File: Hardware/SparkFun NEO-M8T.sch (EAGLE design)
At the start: 51 parts, among them J13 U.FL, J2 Qwiic Right Angle, J4 Qwiic Right Angle, U1 U-BLOX_NEO-M9N, U2 3.3V

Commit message: Some updates to the design (heh)
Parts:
- JP15: device SparkFun-Connectors:CONN_041X04_NO_SILK -> SparkFun-Connectors:CONN_05NO_SILK
- U1: value U-BLOX_NEO-M9N -> U-BLOX_NEO-M8T; device SparkFun-GPS:U-BLOX_NEO-M9N -> SparkFun-GPS:U-BLOX_NEO-M8T
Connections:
- net SCL_LV renamed N$13
- net SDA_LV renamed N$3
- removed net !SAFE: JP15.2, U1.!SAFEBOOT!
- removed net INT: JP15.1, U1.EXT_INT
- new net INT0: JP15.2, U1.EXTINT0
- new net INT1: JP15.1, U1.EXTINT1
- new net TP2/!SAFE: JP15.3, U1.TP2/!SAFEBOOT!
- net !RESET: now also JP15.4; no longer JP15.3
- net PPS: now also JP15.5; no longer JP15.4
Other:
- moved on the sheet: R2, R4
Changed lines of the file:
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@@
 <part name="SUPPLY6" library="SparkFun-PowerSymbols" deviceset="3.3V" device=""/>
 <part name="FB1" library="SparkFun-Coils" deviceset="FERRITE_BEAD" device="-0603" value="30Ω/1.8A"/>
-<part name="JP15" library="SparkFun-Connectors" deviceset="CONN_04" device="1X04_NO_SILK"/>
+<part name="JP15" library="SparkFun-Connectors" deviceset="CONN_05" device="NO_SILK"/>
 <part name="SUPPLY10" library="SparkFun-PowerSymbols" deviceset="3.3V" device=""/>
 <part name="J1" library="SparkFun-Connectors" deviceset="CONN_07" device="NO_SILK"/>
 <part name="SUPPLY11" library="SparkFun-PowerSymbols" deviceset="5V" device=""/>
 <part name="LOGO2" library="SparkFun-Aesthetics" deviceset="SFE_LOGO_NAME_FLAME" device=".1_INCH"/>
-<part name="U1" library="SparkFun-GPS" deviceset="U-BLOX_NEO-M9N" device=""/>
+<part name="U1" library="SparkFun-GPS" deviceset="U-BLOX_NEO-M8T" device=""/>
 <part name="PWR\" library="SparkFun-Jumpers" deviceset="JUMPER-SMT_2_NC_TRACE" device="_SILK" value="JUMPER-SMT_2_NC_TRACE_SILK"/>
 <part name="D3" library="SparkFun-IC-Power" deviceset="PRTR5V0U2" device="F"/>
@@
 </instance>
 <instance part="R3" gate="G$1" x="81.28" y="149.86" smashed="yes">
-<attribute name="NAME" x="76.962" y="150.114" size="1.778" layer="95" font="vector" align="bottom-center"/>
-<attribute name="VALUE" x="85.852" y="150.114" size="1.778" layer="96" font="vector" rot="R180" align="top-center"/>
+<attribute name="NAME" x="76.962" y="147.574" size="1.778" layer="95" font="vector" align="bottom-center"/>
+<attribute name="VALUE" x="85.852" y="147.574" size="1.778" layer="96" font="vector" rot="R180" align="top-center"/>
 </instance>
 <instance part="R6" gate="G$1" x="81.28" y="147.32" smashed="yes">
@@
 <instance part="JP71" gate="G$1" x="233.68" y="27.94" smashed="yes" rot="R270"/>
 <instance part="JP81" gate="G$1" x="236.22" y="27.94" smashed="yes" rot="R270"/>
-<instance part="R2" gate="G$1" x="81.28" y="157.48" smashed="yes">
-<attribute name="NAME" x="77.216" y="158.496" size="1.778" layer="95" font="vector" align="bottom-center"/>
-<attribute name="VALUE" x="85.344" y="158.496" size="1.778" layer="96" font="vector" rot="R180" align="top-center"/>
-</instance>
-<instance part="R4" gate="G$1" x="81.28" y="154.94" smashed="yes">
+<instance part="R2" gate="G$1" x="81.28" y="154.94" smashed="yes">
 <attribute name="NAME" x="76.962" y="152.908" size="1.778" layer="95" font="vector" align="bottom-center"/>
-<attribute name="VALUE" x="85.852" y="152.654" size="1.778" layer="96" font="vector" rot="R180" align="top-center"/>
+<attribute name="VALUE" x="85.598" y="152.908" size="1.778" layer="96" font="vector" rot="R180" align="top-center"/>
+</instance>
+<instance part="R4" gate="G$1" x="81.28" y="152.4" smashed="yes">
+<attribute name="NAME" x="76.962" y="150.368" size="1.778" layer="95" font="vector" align="bottom-center"/>
+<attribute name="VALUE" x="85.852" y="150.114" size="1.778" layer="96" font="vector" rot="R180" align="top-center"/>
 </instance>
 <instance part="SUPPLY1" gate="G$1" x="30.48" y="165.1" smashed="yes" rot="MR0">
@@
 <attribute name="VALUE" x="219.71" y="91.44" size="1.778" layer="96" font="vector" align="top-left"/>
 </instance>
-<instance part="JP15" gate="J1" x="101.6" y="88.9" smashed="yes" rot="MR0">
-<attribute name="VALUE" x="106.68" y="78.74" size="1.778" layer="96" rot="MR0"/>
-<attribute name="NAME" x="106.68" y="97.282" size="1.778" layer="95" font="vector" rot="MR0"/>
+<instance part="JP15" gate="G$1" x="104.14" y="91.44" smashed="yes" rot="MR0">
+<attribute name="VALUE" x="109.22" y="81.28" size="1.778" layer="96" rot="MR0"/>
+<attribute name="NAME" x="109.22" y="99.822" size="1.778" layer="95" font="vector" rot="MR0"/>
 </instance>
 <instance part="SUPPLY10" gate="G$1" x="124.46" y="96.52" smashed="yes">
@@
 <segment>
 <pinref part="R4" gate="G$1" pin="2"/>
-<wire x1="86.36" y1="154.94" x2="88.9" y2="154.94" width="0.1524" layer="91"/>
-<label x="88.9" y="154.94" size="1.27" layer="95" font="vector" xref="yes"/>
+<wire x1="86.36" y1="152.4" x2="88.9" y2="152.4" width="0.1524" layer="91"/>
+<label x="88.9" y="152.4" size="1.27" layer="95" font="vector" xref="yes"/>
 </segment>
 <segment>
@@
 <segment>
 <pinref part="R2" gate="G$1" pin="2"/>
-<wire x1="86.36" y1="157.48" x2="88.9" y2="157.48" width="0.1524" layer="91"/>
-<label x="88.9" y="157.48" size="1.27" layer="95" font="vector" xref="yes"/>
+<wire x1="86.36" y1="154.94" x2="88.9" y2="154.94" width="0.1524" layer="91"/>
+<label x="88.9" y="154.94" size="1.27" layer="95" font="vector" xref="yes"/>
 </segment>
 <segment>
@@
 </segment>
 <segment>
-<wire x1="96.52" y1="91.44" x2="93.98" y2="91.44" width="0.1524" layer="91"/>
-<label x="93.98" y="91.44" size="1.27" layer="95" font="vector" rot="MR0" xref="yes"/>
-<pinref part="JP15" gate="J1" pin="3"/>
-</segment>
-</net>
-<net name="INT" class="0">
+<wire x1="96.52" y1="93.98" x2="93.98" y2="93.98" width="0.1524" layer="91"/>
+<label x="93.98" y="93.98" size="1.27" layer="95" font="vector" rot="MR0" xref="yes"/>
+<pinref part="JP15" gate="G$1" pin="4"/>
+</segment>
+</net>
+<net name="INT0" class="0">
 <segment>
 <wire x1="66.04" y1="160.02" x2="68.58" y2="160.02" width="0.1524" layer="91"/>
 <label x="68.58" y="160.02" size="1.27" layer="95" font="vector" xref="yes"/>
-<pinref part="U1" gate="G$1" pin="EXT_INT"/>
-</segment>
-<segment>
-<wire x1="96.52" y1="86.36" x2="93.98" y2="86.36" width="0.1524" layer="91"/>
-<label x="93.98" y="86.36" size="1.27" layer="95" font="vector" rot="MR0" xref="yes"/>
-<pinref part="JP15" gate="J1" pin="1"/>
+<pinref part="U1" gate="G$1" pin="EXTINT0"/>
+</segment>
+<segment>
+<wire x1="96.52" y1="88.9" x2="93.98" y2="88.9" width="0.1524" layer="91"/>
+<label x="93.98" y="88.9" size="1.27" layer="95" font="vector" rot="MR0" xref="yes"/>
+<pinref part="JP15" gate="G$1" pin="2"/>
 </segment>
 </net>
@@
 </segment>
 <segment>
-<wire x1="96.52" y1="93.98" x2="93.98" y2="93.98" width="0.1524" layer="91"/>
-<label x="93.98" y="93.98" size="1.27" layer="95" font="vector" rot="MR0" xref="yes"/>
-<pinref part="JP15" gate="J1" pin="4"/>
-</segment>
-<segment>
 <wire x1="20.32" y1="45.72" x2="20.32" y2="48.26" width="0.1524" layer="91"/>
 <label x="20.32" y="48.26" size="1.27" layer="95" font="vector" rot="R90" xref="yes"/>
 <pinref part="PPS" gate="G$1" pin="2"/>
+</segment>
+<segment>
+<wire x1="96.52" y1="96.52" x2="93.98" y2="96.52" width="0.1524" layer="91"/>
+<label x="93.98" y="96.52" size="1.27" layer="95" font="vector" rot="MR0" xref="yes"/>
+<pinref part="JP15" gate="G$1" pin="5"/>
 </segment>
 </net>
@@
 </segment>
 </net>
-<net name="SDA_LV" class="0">
-<segment>
-<pinref part="R2" gate="G$1" pin="1"/>
-<wire x1="76.2" y1="157.48" x2="66.04" y2="157.48" width="0.1524" layer="91"/>
-<pinref part="U1" gate="G$1" pin="SDA/SPI_!CS!"/>
-</segment>
-</net>
-<net name="SCL_LV" class="0">
-<segment>
-<pinref part="R4" gate="G$1" pin="1"/>
-<wire x1="76.2" y1="154.94" x2="66.04" y2="154.94" width="0.1524" layer="91"/>
-<pinref part="U1" gate="G$1" pin="SCL/SPI_CLK"/>
-</segment>
-</net>
-<net name="!SAFE" class="0">
+<net name="TP2/!SAFE" class="0">
 <segment>
 <wire x1="66.04" y1="132.08" x2="68.58" y2="132.08" width="0.1524" layer="91"/>
 <label x="68.58" y="132.08" size="1.27" layer="95" font="vector" xref="yes"/>
-<pinref part="U1" gate="G$1" pin="!SAFEBOOT!"/>
-</segment>
-<segment>
-<wire x1="96.52" y1="88.9" x2="93.98" y2="88.9" width="0.1524" layer="91"/>
-<label x="93.98" y="88.9" size="1.27" layer="95" font="vector" rot="MR0" xref="yes"/>
-<pinref part="JP15" gate="J1" pin="2"/>
+<pinref part="U1" gate="G$1" pin="TP2/!SAFEBOOT!"/>
+</segment>
+<segment>
+<wire x1="96.52" y1="91.44" x2="93.98" y2="91.44" width="0.1524" layer="91"/>
+<label x="93.98" y="91.44" size="1.27" layer="95" font="vector" rot="MR0" xref="yes"/>
+<pinref part="JP15" gate="G$1" pin="3"/>
 </segment>
 </net>
@@
 </segment>
 </net>
+<net name="N$3" class="0">
+<segment>
+<pinref part="U1" gate="G$1" pin="SDA/SPI_!CS!"/>
+<pinref part="R2" gate="G$1" pin="1"/>
+<wire x1="66.04" y1="154.94" x2="76.2" y2="154.94" width="0.1524" layer="91"/>
+</segment>
+</net>
+<net name="N$13" class="0">
+<segment>
+<pinref part="R4" gate="G$1" pin="1"/>
+<pinref part="U1" gate="G$1" pin="SCL/SPI_CLK"/>
+<wire x1="76.2" y1="152.4" x2="66.04" y2="152.4" width="0.1524" layer="91"/>
+</segment>
+</net>
+<net name="INT1" class="0">
+<segment>
+<pinref part="U1" gate="G$1" pin="EXTINT1"/>
+<wire x1="66.04" y1="157.48" x2="68.58" y2="157.48" width="0.1524" layer="91"/>
+<label x="68.58" y="157.48" size="1.27" layer="95" xref="yes"/>
+</segment>
+<segment>
+<pinref part="JP15" gate="G$1" pin="1"/>
+<wire x1="96.52" y1="86.36" x2="93.98" y2="86.36" width="0.1524" layer="91"/>
+<label x="93.98" y="86.36" size="1.27" layer="95" rot="R180" xref="yes"/>
+</segment>
+</net>

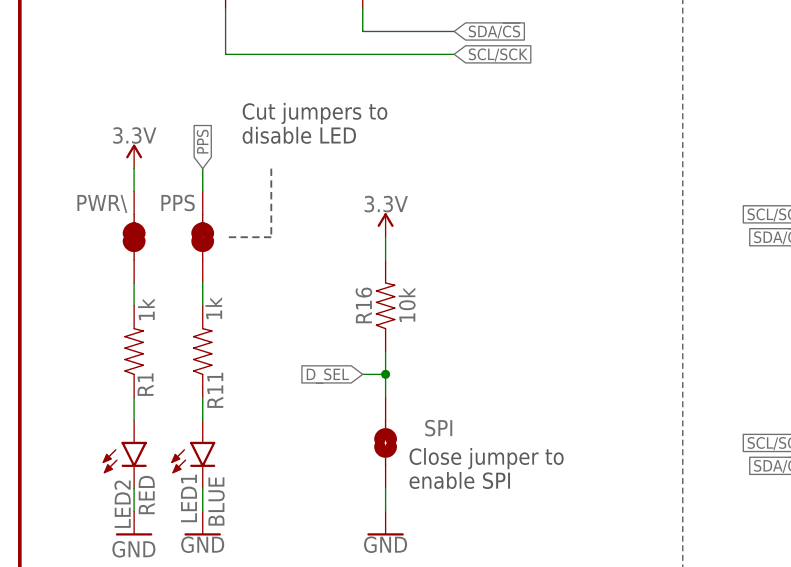
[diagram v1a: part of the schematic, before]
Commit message: Removes 10k from board
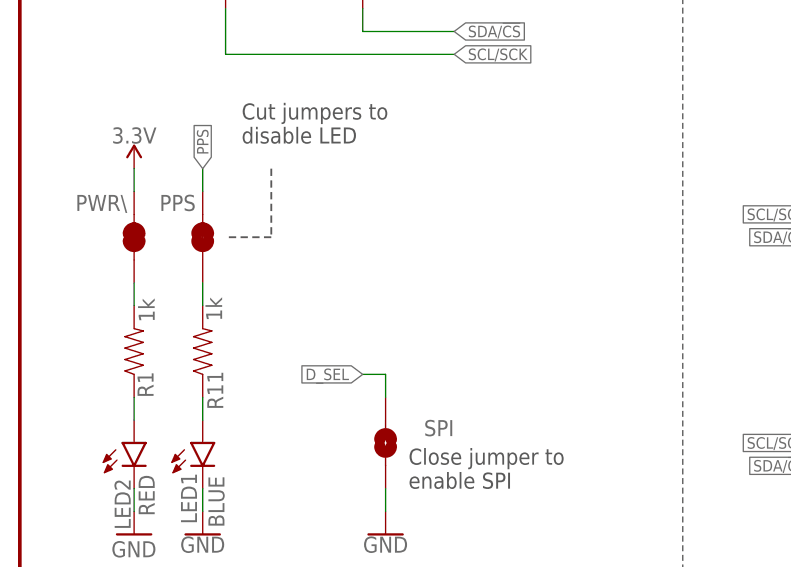
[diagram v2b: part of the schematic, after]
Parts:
- removed R16: 10k, SparkFun-Resistors:10KOHM-0402-1/16W-1%
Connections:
- net 3.3V: no longer R16.2
- net D_SEL: no longer R16.1
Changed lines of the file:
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@@
 <part name="GND9" library="SparkFun-PowerSymbols" deviceset="GND" device=""/>
 <part name="GND17" library="SparkFun-PowerSymbols" deviceset="GND" device=""/>
-<part name="R16" library="SparkFun-Resistors" deviceset="10KOHM" device="-0402-1/16W-1%" value="10k"/>
-<part name="SUPPLY12" library="SparkFun-PowerSymbols" deviceset="3.3V" device=""/>
 </parts>
 <sheets>
@@
 <attribute name="VALUE" x="144.78" y="127" size="1.778" layer="96" font="vector"/>
 </instance>
-<instance part="R16" gate="G$1" x="40.64" y="33.02" smashed="yes" rot="R90">
-<attribute name="NAME" x="39.116" y="33.02" size="1.778" layer="95" font="vector" rot="R90" align="bottom-center"/>
-<attribute name="VALUE" x="42.164" y="33.02" size="1.778" layer="96" font="vector" rot="R90" align="top-center"/>
-</instance>
-<instance part="SUPPLY12" gate="G$1" x="40.64" y="40.64" smashed="yes">
-<attribute name="VALUE" x="40.64" y="43.434" size="1.778" layer="96" font="vector" align="bottom-center"/>
-</instance>
 </instances>
 <busses>
@@
 <pinref part="P+1" gate="G$1" pin="3.3V"/>
 <wire x1="12.7" y1="45.72" x2="12.7" y2="48.26" width="0.1524" layer="91"/>
-</segment>
-<segment>
-<pinref part="R16" gate="G$1" pin="2"/>
-<wire x1="40.64" y1="38.1" x2="40.64" y2="40.64" width="0.1524" layer="91"/>
-<pinref part="SUPPLY12" gate="G$1" pin="3.3V"/>
 </segment>
 </net>
@@
 </segment>
 <segment>
-<pinref part="R16" gate="G$1" pin="1"/>
 <pinref part="SPI" gate="G$1" pin="2"/>
-<wire x1="40.64" y1="27.94" x2="40.64" y2="25.4" width="0.1524" layer="91"/>
 <wire x1="40.64" y1="25.4" x2="40.64" y2="22.86" width="0.1524" layer="91"/>
 <wire x1="38.1" y1="25.4" x2="40.64" y2="25.4" width="0.1524" layer="91"/>
-<junction x="40.64" y="25.4"/>
 <label x="38.1" y="25.4" size="1.27" layer="95" rot="R180" xref="yes"/>
 </segment>
